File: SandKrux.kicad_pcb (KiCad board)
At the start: 2 copper layers, 58.3 x 98.2 mm, 158 parts, among them CN2 1.25mm-2P socket, IC1 TROPIC01_chip, Q1 S8050, Q2 SI2301CDS-T1-GE3, SW1 TL3330AF130QG, SW2 TL3330AF130QG, SW3 TL3330AF130QG, SW4 TL3330AF130QG, SW5 TL3330AF130QG, U1 K210_C913414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

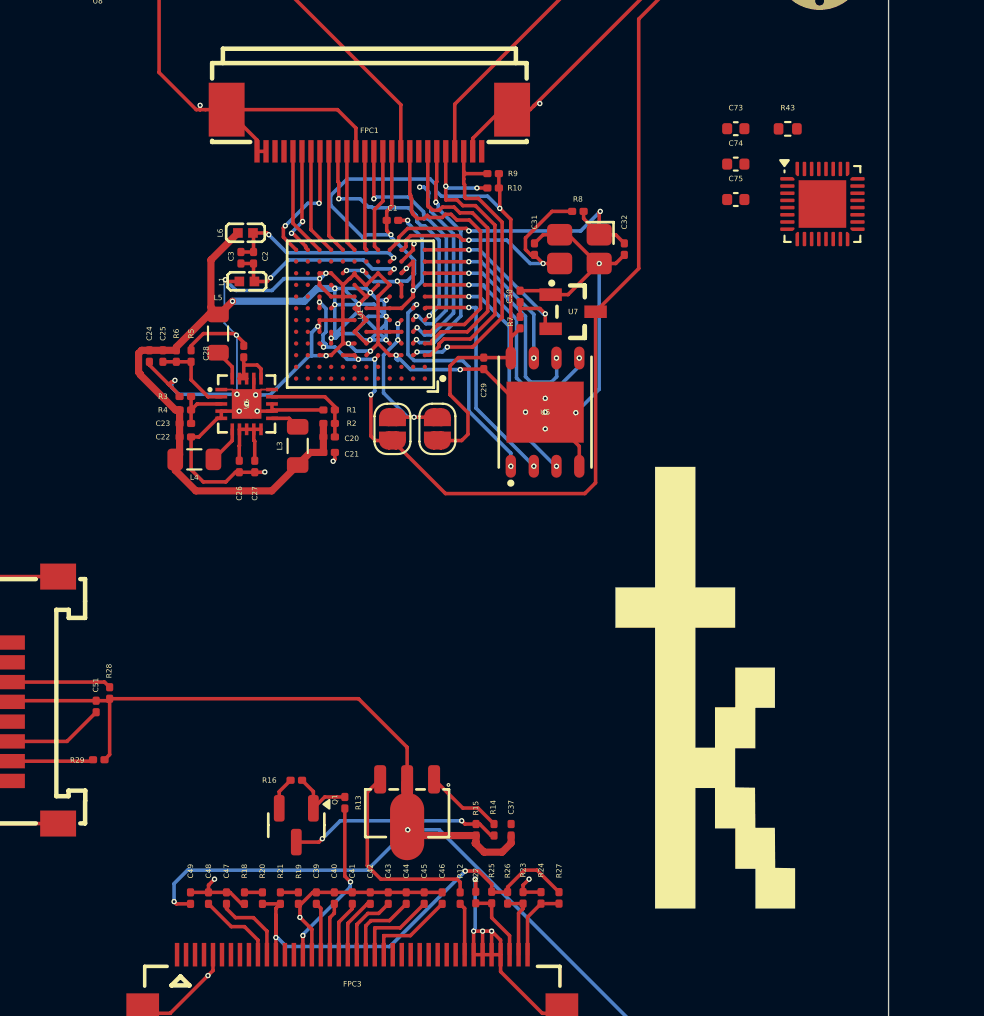
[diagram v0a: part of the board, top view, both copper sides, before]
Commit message: fios e vias lcd toutch botoes e o q mais estava conectado ao modulo m2 alem da coexao m2 com k210
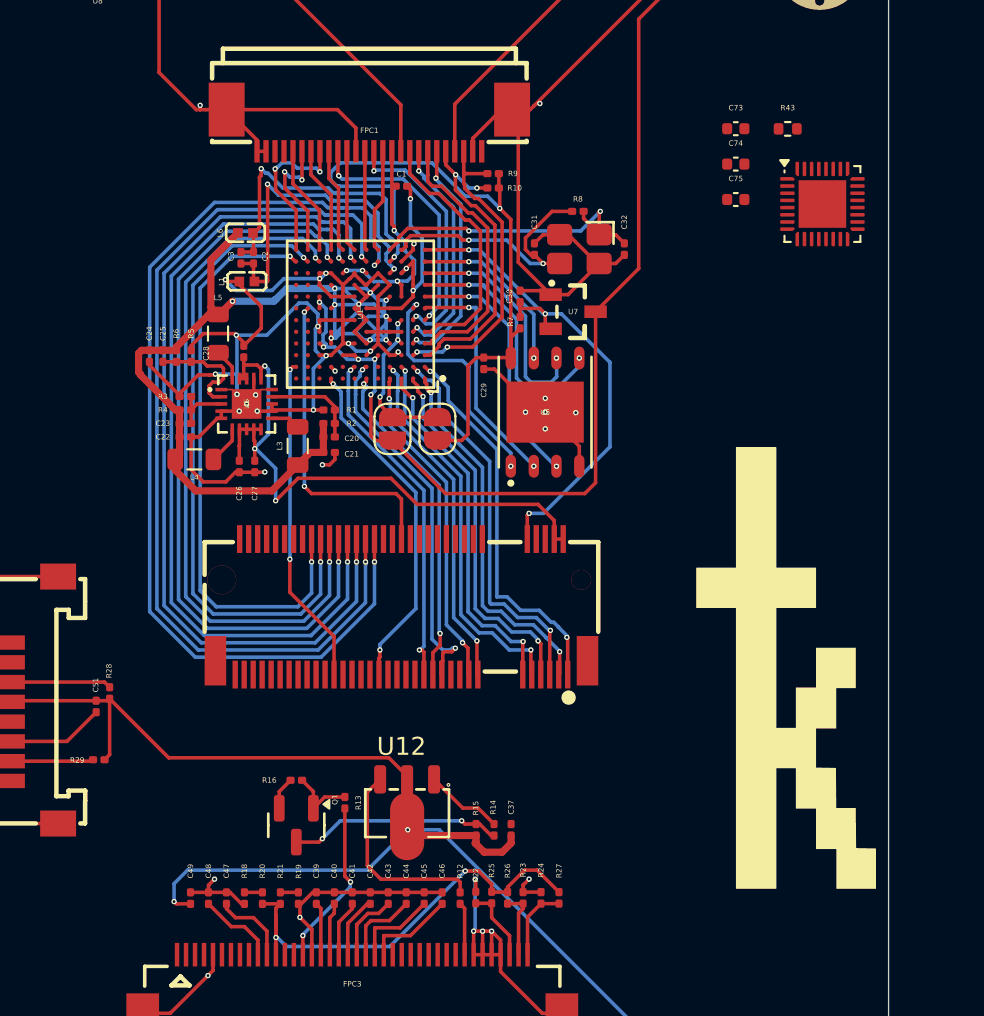
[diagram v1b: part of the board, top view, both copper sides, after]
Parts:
- added U12: PCIE-67P42H, easyeda2kicad:PCIE-SMD_75P-P0.50_HYC01B-05NGFF-420, F.Cu at (111.4, 128.1)
- moved G*** 4.63 mm to (132.8, 131.5)
- moved C1 1.96 mm to (111.4, 104.7)
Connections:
- C26 pad 2: /k210/5V -> /5V
- C27 pad 2: /k210/5V -> /5V
- C28 pad 2: /k210/5V -> /5V
- C30 pad 2: /k210/RST -> /RST
- FPC3 pad 10: /LCD_DC -> Net-(FPC3-Pad10)
- FPC3 pad 11: /LCD_WR -> Net-(FPC3-Pad11)
- FPC3 pad 17: /LCD_D0 -> Net-(FPC3-Pad17)
- FPC3 pad 18: /LCD_D1 -> Net-(FPC3-Pad18)
- FPC3 pad 19: /LCD_D2 -> Net-(FPC3-Pad19)
- FPC3 pad 20: /LCD_D3 -> Net-(FPC3-Pad20)
- FPC3 pad 21: /LCD_D4 -> Net-(FPC3-Pad21)
- FPC3 pad 22: /LCD_D5 -> Net-(FPC3-Pad22)
- FPC3 pad 23: /LCD_D6 -> Net-(FPC3-Pad23)
- FPC3 pad 24: /LCD_D7 -> Net-(FPC3-Pad24)
- R7 pad 2: /k210/RST -> /RST
- U1 pad A1: /k210/IO_37 -> /LCD_RST
- U1 pad A2: /k210/IO_36 -> /LCD_CS
- U1 pad A3: /k210/I2S2_SDI -> /I2S2_SDI
- U1 pad A4: /k210/IO_33 -> /PIN23
- U1 pad A6: /k210/IO_29 -> /USB_D-
- U1 pad A9: /k210/IO_23 -> /KEY1
- U1 pad B1: /k210/LCD_WR -> /LCD_WR
- U1 pad B12: /k210/BOOT -> /BOOT
- U1 pad B2: /k210/LCD_DC -> /LCD_DC
- U1 pad B3: /k210/I2S2_SDO -> /I2S2_SDOD
- U1 pad B4: /k210/IO_32 -> /PIN21
- U1 pad B6: /k210/IO_28 -> /USB_D+
- U1 pad B7: /k210/IO_26 -> /SPI1_CS_TF
- U1 pad G11: /k210/IO_6 -> /SPI1_MISO
- U1 pad J11: /k210/IO_2 -> unconnected-(U1-IO_2-PadJ11)
- U1 pad J12: /k210/IO_3 -> unconnected-(U1-IO_3-PadJ12)
- U1 pad K11: /k210/IO_0 -> unconnected-(U1-IO_0-PadK11)
- U1 pad K12: /k210/IO_1 -> unconnected-(U1-IO_1-PadK12)
- U1 pad L10: /k210/SPI0_D2 -> /LCD_D2
- U1 pad L11: /k210/SPI0_D1 -> /LCD_D1
- U1 pad L12: /k210/SPI0_D0 -> /LCD_D0
- U1 pad L5: /k210/SPI0_D8 -> /LCD_D7
- U1 pad L6: /k210/SPI0_D7 -> /LCD_D6
- U1 pad L7: /k210/SPI0_D5 -> /LCD_D5
- U1 pad L8: /k210/SPI0_D4 -> /LCD_D4
- U1 pad L9: /k210/SPI0_D3 -> /LCD_D3
- U1 pad M1: /k210/RST -> /RST
- U6 pad 10: /k210/5V -> /5V
- U6 pad 16: /k210/5V -> /5V
- U6 pad 18: /k210/5V -> /5V
- U6 pad 19: /k210/5V -> /5V
- U6 pad 7: /k210/5V -> /5V
- U6 pad 8: /k210/5V -> /5V
- U6 pad 9: /k210/5V -> /5V
- U7 pad 2: /k210/RST -> /RST
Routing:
- net /LCD_D7: track 5.04 -> 60.0 mm, vias 0 -> 2
- net /LCD_D6: track 4.80 -> 56.2 mm, vias 0 -> 2
- net /LCD_D5: track 4.36 -> 52.7 mm, vias 0 -> 2
- net /LCD_D4: track 3.90 -> 49.2 mm, vias 0 -> 2
- net /LCD_D3: track 3.44 -> 45.5 mm, vias 0 -> 2
- net /LCD_D2: track 3.14 -> 42.1 mm, vias 0 -> 2
- net /LCD_D1: track 2.93 -> 38.9 mm, vias 0 -> 2
- net /5V: track 13.9 -> 49.6 mm, vias 2 -> 5
- net /LCD_D0: track 2.93 -> 35.8 mm, vias 0 -> 2
- net /RST: track 0.00 -> 28.5 mm, vias 0 -> 3
- net /LCD_WR: track 4.35 -> 25.9 mm, vias 0 -> 2
- net /LCD_DC: track 4.40 -> 25.9 mm, vias 0 -> 2
- net /I2S2_SDOD: track 0.00 -> 21.3 mm, vias 0 -> 2
- net /USB_D+: track 2.99 -> 23.9 mm, vias 0 -> 2
- net /LCD_RST: track 9.36 -> 30.0 mm, vias 2 -> 4
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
